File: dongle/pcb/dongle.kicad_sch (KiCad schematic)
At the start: 30 parts, among them U2 MAX3421EEHJ_T, U3 ESP32-S3-MINI-1, U4 TPS2051BDBVR, U5 NCP167BMX330TBG, X1 SMD-3225_4P12M12PF10PPM

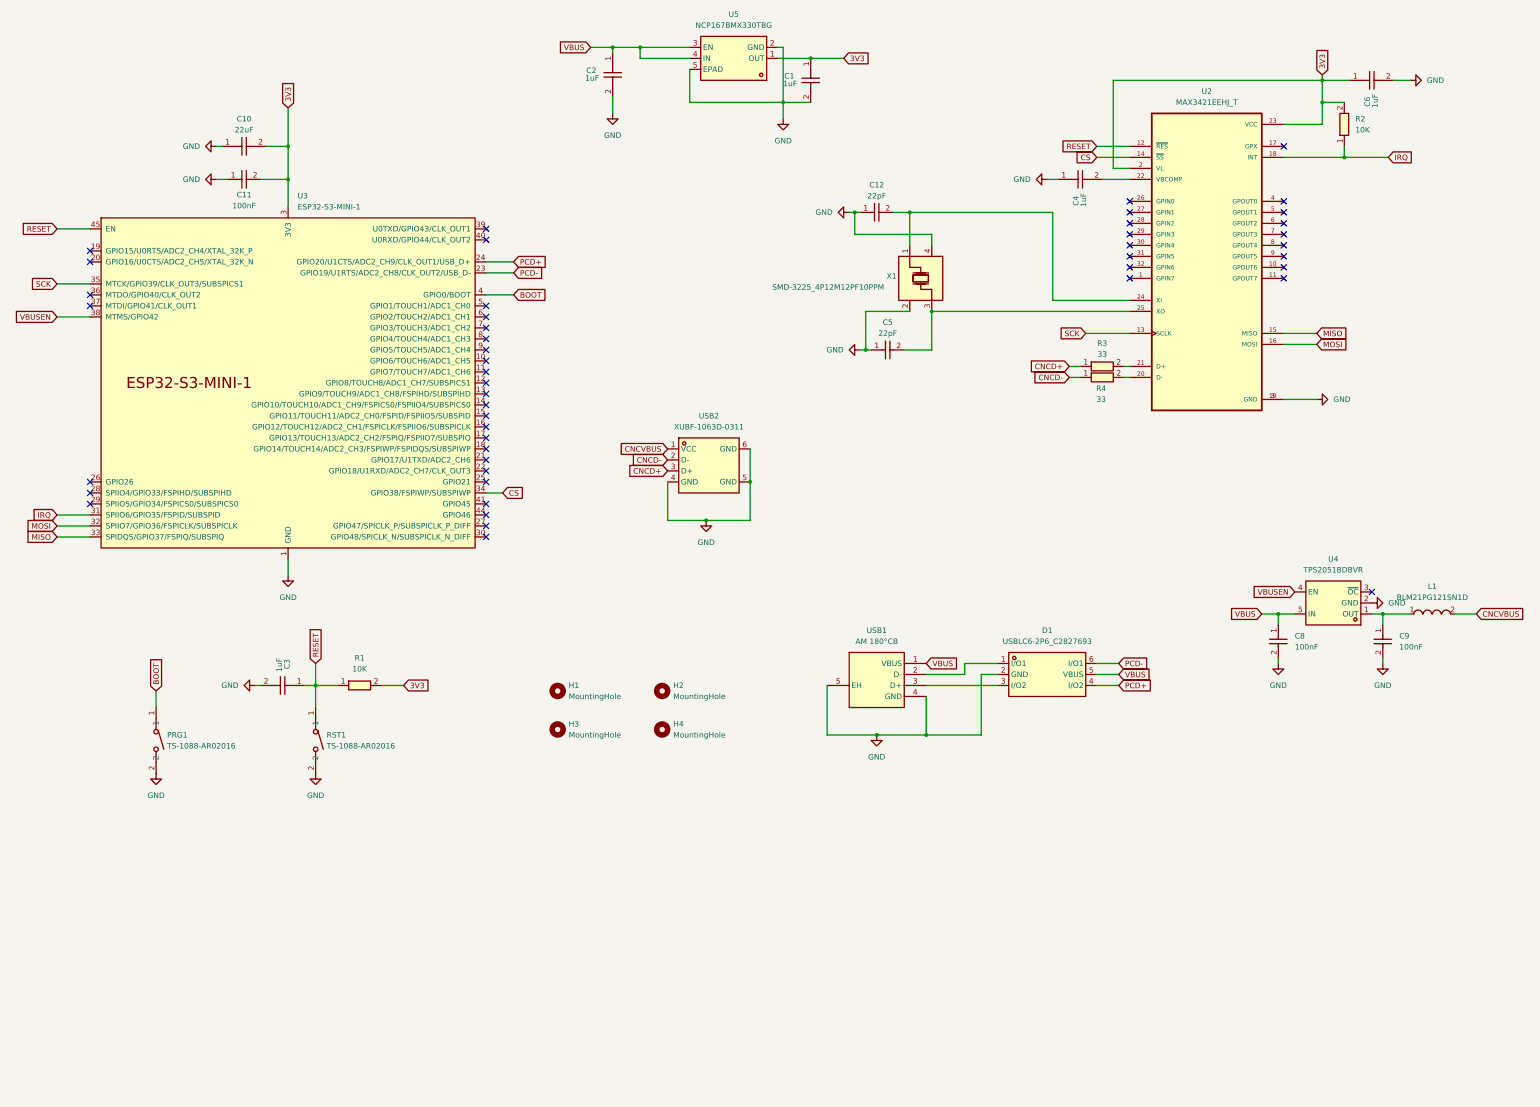
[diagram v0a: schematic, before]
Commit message: use ch9102f for pc usb
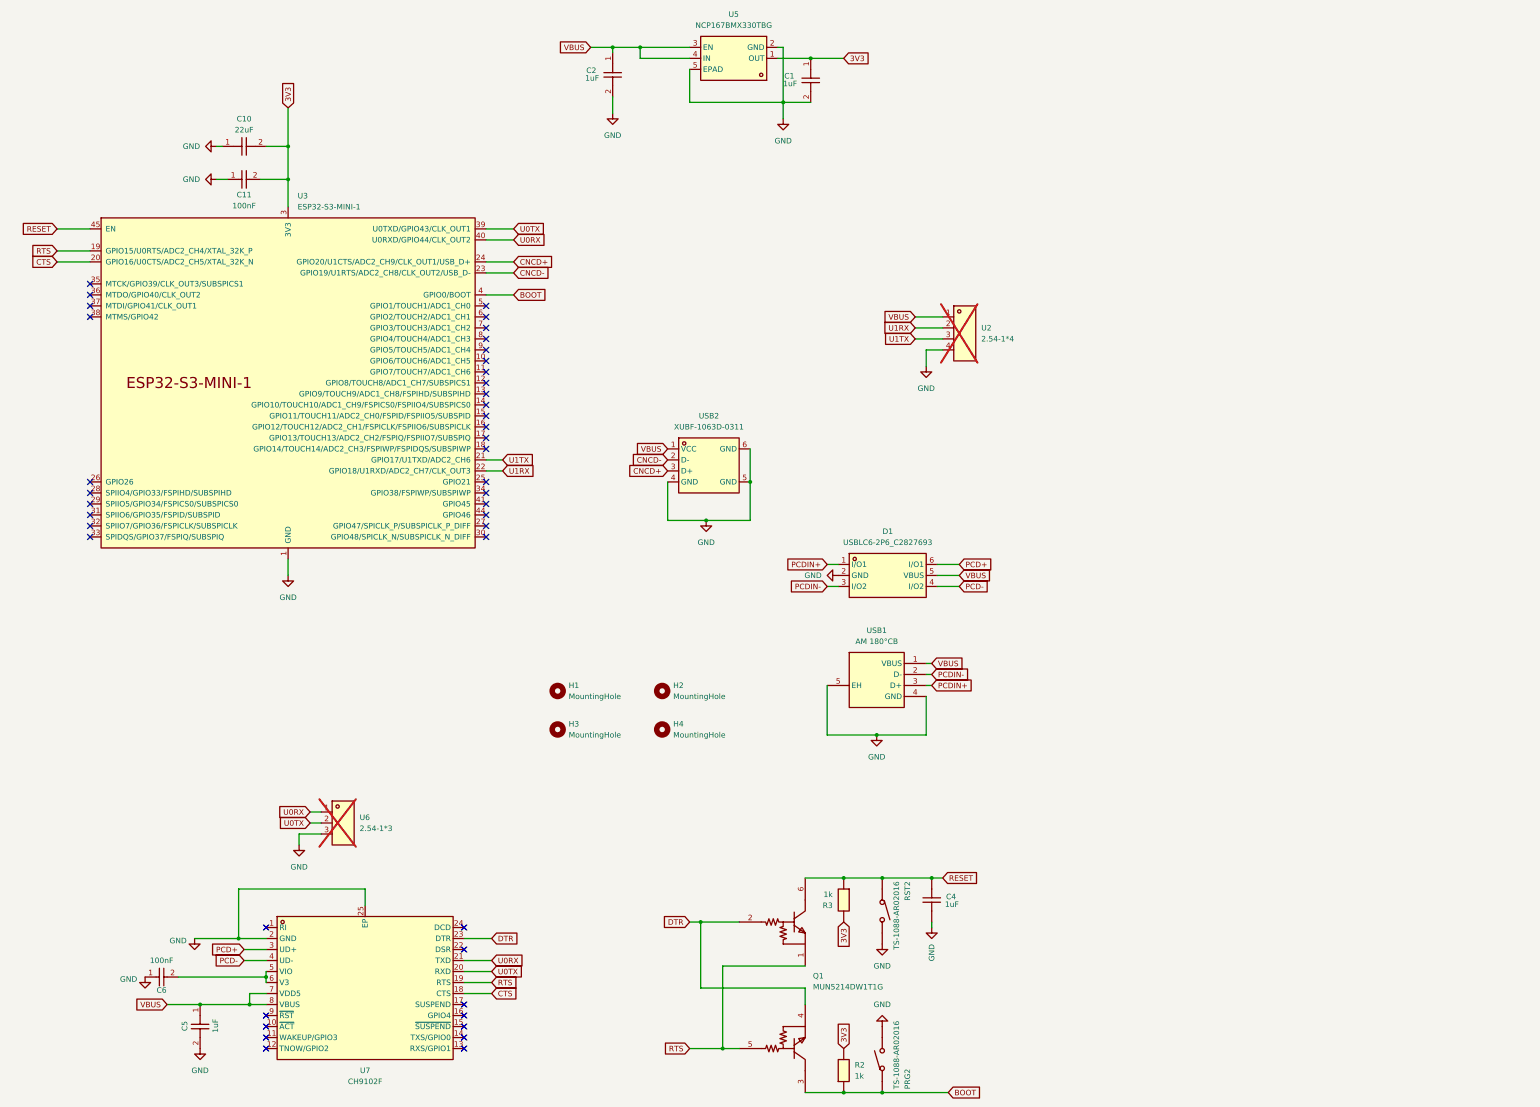
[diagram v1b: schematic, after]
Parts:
- removed C12, C5: 22pF, dongle:C0402, symbol dongle:0402CG220J500NT
- removed C3, C6: 1uF, dongle:C0402, symbol dongle:CL05A105KA5NQNC
- removed C8, C9: 100nF, dongle:C0402, symbol dongle:CL05B104KO5NNNC
- removed L1: BLM21PG121SN1D, dongle:L0805, symbol dongle:BLM21PG121SN1D
- removed PRG1, RST1: TS-1088-AR02016, dongle:SW-SMD_L3.9-W3.0-P4.45, symbol dongle:TS-1088-AR02016
- removed R1, R2: 10K, dongle:R0402, symbol dongle:0402WGF1002TCE
- removed R3, R4: 33, dongle:R0402, symbol dongle:0402WGF330JTCE
- removed U2: MAX3421EEHJ_T, MAX3421EEHJ_T:QFP50P700X700X120-32N, symbol MAX3421EEHJ_T:MAX3421EEHJ_T
- removed U4: TPS2051BDBVR, dongle:SOT-23-5_L3.0-W1.7-P0.95-LS2.8-BR, symbol dongle:TPS2051BDBVR
- removed X1: SMD-3225_4P12M12PF10PPM, dongle:CRYSTAL-SMD_4P-L3.2-W2.5-BL, symbol dongle:SMD-3225_4P12M12PF10PPM
- added C5: 1uF, dongle:C0402, symbol dongle:CL05A105KA5NQNC
- added C6: 100nF, dongle:C0402, symbol dongle:CL05B104KO5NNNC
- added PRG2, RST2: TS-1088-AR02016, dongle:SW-SMD_L3.9-W3.0-P4.45, symbol dongle:TS-1088-AR02016
- added Q1: MUN5214DW1T1G, dongle:SOT-363_L2.0-W1.3-P0.65-LS2.1-TL, symbol dongle:MUN5214DW1T1G
- added R2, R3: 1k, dongle:R0201, symbol dongle:ERA1AEB102C
- added U2: 2.54-1*4, dongle:HDR-TH_4P-P2.54-V-M-1, symbol dongle:2.54-1*4
- added U6: 2.54-1*3, dongle:HDR-TH_3P-P2.54-V-M-1, symbol dongle:2.54-1*3
- added U7: CH9102F, dongle:QFN-24_L4.0-W4.0-P0.50-BL-EP2.5, symbol dongle:CH9102F
- U3: footprint PCM_Espressif:ESP32-S3-MINI-1 -> dongle:ESP32-S3-MINI-1; symbol PCM_Espressif:ESP32-S3-MINI-1 -> dongle:ESP32-S3-MINI-1
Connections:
- net CNCVBUS is gone; now on net VBUS: USB2.1 (VCC)
- net 3V3: now also R2.2, R3.2
- net BOOT: now also PRG2.1, Q1.3, R2.1
- net CNCD+: now also U3.24 (GPIO20/U1CTS/ADC2_CH9/CLK_OUT1/USB_D+)
- net CNCD-: now also U3.23 (GPIO19/U1RTS/ADC2_CH8/CLK_OUT2/USB_D-)
- net GND: now also C4.2, C5.2, C6.1, PRG2.2, RST2.2, U2.4, U6.3, U7.2 (GND), U7.25 (EP); no longer C4.1
- net PCD+: now also D1.6 (I/O1), U7.3 (UD+); no longer D1.4 (I/O2), U3.24 (GPIO20/U1CTS/ADC2_CH9/CLK_OUT1/USB_D+)
- net PCD-: now also D1.4 (I/O2), U7.4 (UD-); no longer D1.6 (I/O1), U3.23 (GPIO19/U1RTS/ADC2_CH8/CLK_OUT2/USB_D-)
- net RESET: now also C4.1, Q1.6, R3.1, RST2.1
- net VBUS: now also C5.1, U2.1, U7.7 (VDD5), U7.8 (VBUS)
- net PCDIN+: now reaches D1.1 (I/O1)
- net PCDIN+: now also USB1.3 (D+); no longer USB1.2 (D-)
- net PCDIN-: now reaches D1.3 (I/O2)
- net PCDIN-: now also USB1.2 (D-); no longer USB1.3 (D+)
- net RTS: now reaches U3.19 (GPIO15/U0RTS/ADC2_CH4/XTAL_32K_P)
- net RTS: now also Q1.1, Q1.5, U7.19 (RTS)
- net CTS: now reaches U3.20 (GPIO16/U0CTS/ADC2_CH5/XTAL_32K_N)
- net CTS: now also U7.18 (CTS)
- net U1TX: now reaches U3.21 (GPIO17/U1TXD/ADC2_CH6)
- net U1TX: now also U2.3
- net U1RX: now reaches U3.22 (GPIO18/U1RXD/ADC2_CH7/CLK_OUT3)
- net U1RX: now also U2.2
- net U0TX: now reaches U3.39 (U0TXD/GPIO43/CLK_OUT1)
- net U0TX: now also U6.2, U7.20 (RXD)
- net U0RX: now reaches U3.40 (U0RXD/GPIO44/CLK_OUT2)
- net U0RX: now also U6.1, U7.21 (TXD)
- net CS: no longer names the net of U3.34 (GPIO38/FSPIWP/SUBSPIWP)
- net IRQ: no longer names the net of U3.31 (SPIIO6/GPIO35/FSPID/SUBSPID)
- net MISO: no longer names the net of U3.33 (SPIDQS/GPIO37/FSPIQ/SUBSPIQ)
- net MOSI: no longer names the net of U3.32 (SPIIO7/GPIO36/FSPICLK/SUBSPICLK)
- net SCK: no longer names the net of U3.35 (MTCK/GPIO39/CLK_OUT3/SUBSPICS1)
- net VBUSEN: no longer names the net of U3.38 (MTMS/GPIO42)
- new net: C6.2, U7.5 (VIO), U7.6 (V3)
- new net DTR: Q1.2, Q1.4, U7.23 (DTR)
- no-connect marks 48 -> 42
